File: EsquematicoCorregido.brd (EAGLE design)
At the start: 100 x 80 mm, 42 parts, among them IC1 OPA991TIDCKR, IC10 MCP73831T-2ACI_OT, IC2 AD8226ARZ-RL, IC3 OPA991TIDCKR, IC4 ESP32-S3-WROOM-1-N16R8, IC5 OPA991TIDCKR, IC6 MAX30102EFD+T, IC7 LP38692MP-3.3_NOPB, IC8 LP38692MP-1.8_NOPB, IC9 REF2033AIDDCT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

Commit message: ultimas actualizaciones
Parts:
- removed C7: C0805J104K1RACAUTO, C0805J104K1RACAUTO:CAPC2012X140N
- removed U1: DM-OLED096-636, DM-OLED096-636:MODULE_DM-OLED096-636
- added SV1: (no value), con-lstb:MA04-1
- C2, C5, C6: value QXK2E475KTP -> (none); device QXK2E475KTP:QXK2E475KTP -> rcl:C0805
- C4: value C2220X205K1RLCAUTO -> (none); device C2220X205K1RLCAUTO:CAPC5950X340N -> rcl:C0805
- C8: value C0805J104K1RACAUTO -> (none); device C0805J104K1RACAUTO:CAPC2012X140N -> rcl:C0805
- moved C8 243.1 mm to (-149.9, -113.0)
- moved S4 238.7 mm to (40.6, 64.8)
- moved S3 234.8 mm to (40.6, 73.7)
- moved C4 216.6 mm to (-149.9, -102.9)
- moved C6 207.9 mm to (-149.9, -108.0)
- moved C5 189.7 mm to (-149.9, -118.1)
- moved POWER 173.4 mm to (48.3, 8.89)
- moved BATT 168.5 mm to (30.5, 10.2)
- moved C2 158.6 mm to (-149.9, -97.8)
- moved IC5 114.4 mm to (33.0, 40.6)
- moved J1 104.2 mm to (2.16, 55.4), turned to 270 degrees
- moved IC10 96.0 mm to (19.1, 7.62)
- moved IC3 95.2 mm to (25.4, 40.6)
- moved IC8 52.1 mm to (21.6, 19.1)
- moved IC7 49.7 mm to (36.8, 19.1)
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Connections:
- new net N$21: SV1.1
- net +3V3: now also C4.1, C6.1, SV1.2; no longer C6.2, C8.2, U1.2
- net EN: now also S3.3
- net GND: now also C5.2, C8.2, S3.1, S4.1; no longer C5.1, C7.1, U1.1
- net IO0: now also S4.3
- net N$2: now also C12.2; no longer C2.2
- net N$3: now also C12.1; no longer C2.1
- net N$4: now also C2.2; no longer C4.2
- net N$9: now also C4.2, C6.2; no longer C6.1, C8.1
- net SCL_DSP: now also SV1.4; no longer U1.3
- net SDA_DSP: now also SV1.3; no longer U1.4
- net VDD: now also C5.1, C8.1; no longer C5.2, C7.2
- net VSS: now also C2.1; no longer C4.1
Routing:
- net +3V3: track 18.5 -> 2.50 mm
- net N$3: track 3.81 -> 0.00 mm
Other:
- board size 100 x 80 mm -> 70.9 x 80 mm

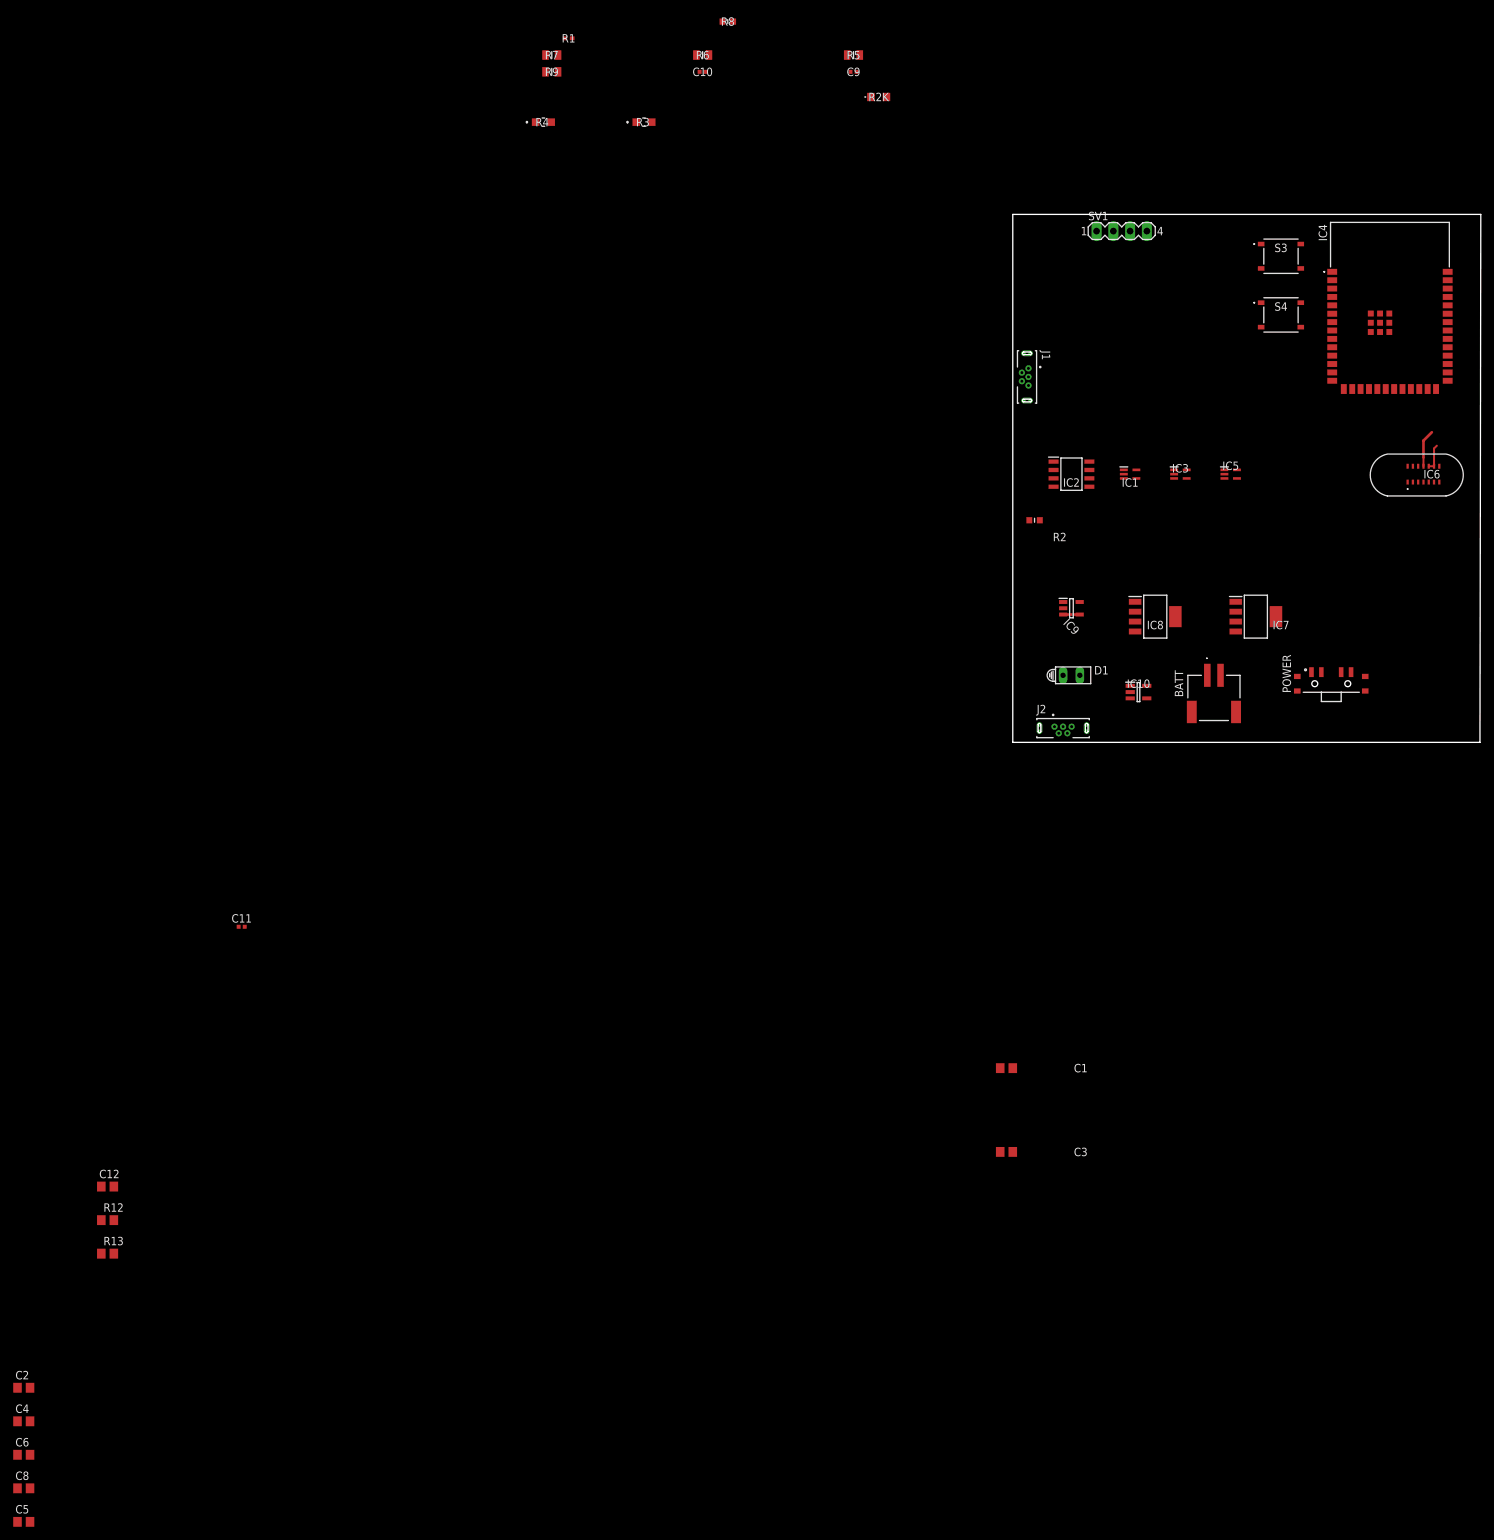
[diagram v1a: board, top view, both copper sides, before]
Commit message: fix: PCB and schematic errors fixed
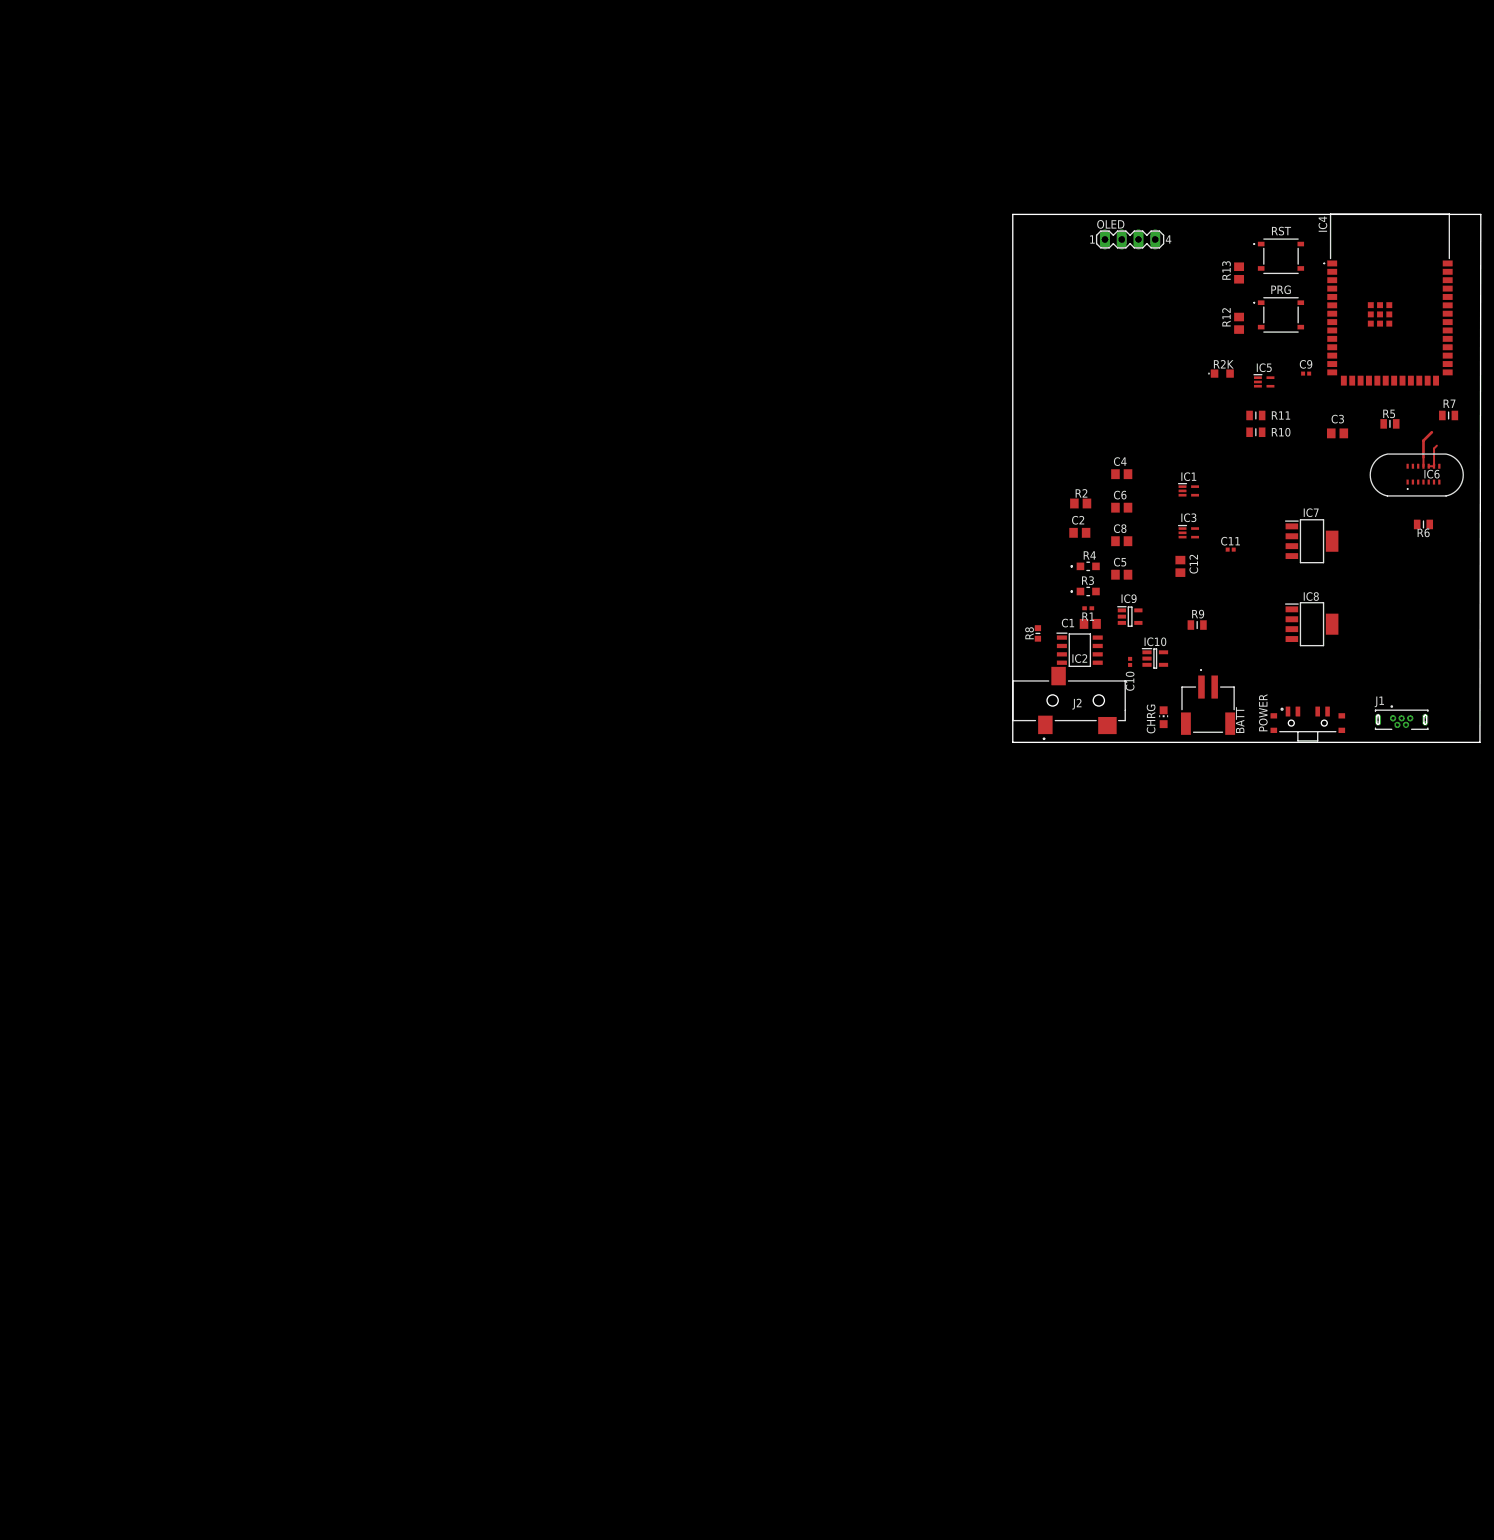
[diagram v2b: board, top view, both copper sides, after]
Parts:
- removed D1: HLMP6, display-hp:HLMP6
- removed SV1: (no value), con-lstb:MA04-1
- added CHRG: (no value), led:CHIP-LED0805
- added OLED: (no value), con-lstb:MA04-1
- added R10, R11: CRCW0805220RFKTAHP, CRCW0805220RFKTAHP:RESC2012X60N
- J2: value USB3131-30-0230-A_REVB -> SJ-3523-SMT-TR; device USB3131-30-0230-A_REVB:GCT_USB3131-30-0230-A_REVB -> SJ-3523-SMT-TR:SJ3523SMTTR
- R2: value RN73H1JTTD1043B50 -> (none); device RN73H1JTTD1043B50:RESC1608X55N -> rcl:R0805
- moved R13 226.9 mm to (34.3, 71.1), turned to 270 degrees
- moved C4 219.7 mm to (16.5, 40.6)
- moved C5 219.7 mm to (16.5, 25.4)
- moved C6 219.7 mm to (16.5, 35.6)
- moved C8 219.7 mm to (16.5, 30.5)
- moved R12 218.8 mm to (34.3, 63.5), turned to 90 degrees
- moved C2 205.9 mm to (10.2, 31.8)
- moved C12 187.8 mm to (25.4, 26.7), turned to 270 degrees
- moved C11 160.4 mm to (33.0, 29.2)
- moved R7 146.5 mm to (66.0, 49.5)
- moved R6 130.3 mm to (62.2, 33.0), turned to 180 degrees
- moved R9 128.8 mm to (27.9, 17.8)
- moved C3 119.9 mm to (49.2, 46.8), turned to 180 degrees
- moved R1 116.9 mm to (11.4, 20.3), turned to 180 degrees
- moved C10 110.4 mm to (17.8, 12.2), turned to 270 degrees
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- renumbered S3 to RST, S4 to PRG
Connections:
- removed net 5V: J2.1
- removed net N$15: IC2.4
- removed net N$16: D1.K, R9.2
- new net INA+: IC2.4, J2.3
- new net INA-: IC2.1, J2.2
- new net N$5: IC5.4, R10.1, R11.1
- net +3V3: now also OLED.2; no longer J1.1, SV1.2
- net +5V: now also CHRG.A, J1.1; no longer D1.A
- net GND: now also R11.2; no longer J2.5, J2.S1, J2.S2
- net N$14: now also CHRG.C, R9.2; no longer IC2.1
- net N$21: now also OLED.1; no longer SV1.1
- net OUT-ADC: now also R10.2
- net SCL_DSP: now also OLED.4; no longer SV1.4
- net SDA_DSP: now also OLED.3; no longer SV1.3
- net VSS: now also J2.1
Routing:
- net +3V3: track 2.50 -> 0.00 mm

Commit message: Avance PCB
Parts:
- removed J1: USB3131-30-0230-A_REVB, USB3131-30-0230-A_REVB:GCT_USB3131-30-0230-A_REVB
- removed R2K: ERJ-UP6D2001V, ERJ-UP6D2001V:ERJUP6
- added J3: USB4216-03-A, USB4216-03-A:USB421603A
- added R14, R15, R16: (no value), rcl:R0805
- C10, C11, C9: value GRM155C80G106ME18D -> (none); device GRM155C80G106ME18D:CAPC1005X70N -> rcl:C0805
- R1: value RN73H1ETTP4812D25 -> (none); device RN73H1ETTP4812D25:RESC1005X40N -> rcl:R0805
- R9: value CRCW0805220RFKTAHP -> (none); device CRCW0805220RFKTAHP:RESC2012X60N -> rcl:R0805
- moved R5 3.97 mm to (61.1, 48.8), turned to 270 degrees
- moved IC7 3.81 mm to (45.3, 26.7)
- moved IC8 2.54 mm to (45.3, 15.4)
- moved C10 1.02 mm to (16.8, 12.1), turned to 90 degrees
- moved R7 0.97 mm to (65.7, 48.6), turned to 270 degrees
- moved C11 0.80 mm to (32.8, 28.4)
- moved C9 0.51 mm to (44.5, 55.4)
- moved R1 0.38 mm to (11.8, 20.3), turned to 0 degrees
- moved R12 0.38 mm to (34.3, 63.9)
- moved R13 0.36 mm to (34.0, 70.9)
- turned IC6 to 270 degrees
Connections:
- removed net N$10: IC4.3
- new net N$16: J3.A5, R15.1
- new net N$19: J3.B5, R16.2
- net +3V3: now also R12.2, R13.2
- net +5V: now also C9.1, J3.A4, J3.B4; no longer C9.2, J1.1
- net 3V3: now also C11.2; no longer C11.1, R12.2, R13.2
- net BATT+: now also C10.1; no longer C10.2
- net D+: now also J3.A6, J3.B6; no longer J1.3
- net D-: now also J3.A7, J3.B7; no longer J1.2
- net EN: now also IC4.3
- net GND: now also C10.2, C11.1, C9.2, J3.A1, J3.B1, J3.G1, J3.G2, J3.G3, J3.G4, R14.1, R15.2, R16.1; no longer C10.1, C11.2, C9.1, J1.5, J1.S1, J1.S2, R2K.1
- net N$17: now also R14.2; no longer R2K.2
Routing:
- net EN: track 0.00 -> 16.1 mm
- net VDD: track 5.68 -> 0.00 mm
- net IO0: track 0.00 -> 5.25 mm
- net N$9: track 4.10 -> 0.00 mm
- net N$15: track 0.00 -> 1.78 mm
- added copper zone on layer 1, net GND
- added copper zone on layer 16, net GND

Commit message: modificaciones PCB
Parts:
- moved C9 44.3 mm to (30.1, 13.5)
- moved R14 43.5 mm to (36.8, 12.7), turned to 270 degrees
- moved C11 37.6 mm to (23.0, 64.8), turned to 90 degrees
- moved C3 32.4 mm to (19.0, 35.1)
- moved C5 29.6 mm to (45.5, 31.4), turned to 180 degrees
- moved C8 29.1 mm to (45.5, 27.7), turned to 180 degrees
- moved C4 29.0 mm to (45.5, 38.9)
- moved C6 29.0 mm to (45.5, 35.3)
- moved OLED 25.4 mm to (19.1, 50.8)
- moved IC1 20.4 mm to (6.35, 39.4)
- moved C12 17.4 mm to (8.64, 31.4), turned to 0 degrees
- moved IC5 17.0 mm to (30.5, 39.4)
- moved R3 15.3 mm to (12.7, 38.1)
- moved R1 14.7 mm to (10.5, 34.9)
- moved R11 14.2 mm to (34.3, 35.6)
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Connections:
- net VDD renamed +1V8
- removed net N$21: OLED.1
- net GND: now also OLED.1
- net OUTFILT: no longer IC4.20
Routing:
- net +3V3: track 0.00 -> 111.3 mm, vias 0 -> 2
- net SDA_DSP: track 0.00 -> 47.3 mm
- net +1V8: track 0.00 -> 45.1 mm, vias 0 -> 2
- net SDA: track 0.00 -> 40.7 mm
- net SCL_DSP: track 0.00 -> 37.4 mm, vias 0 -> 2
- net IO0: track 5.25 -> 42.3 mm, vias 0 -> 2
- net N$12: track 0.00 -> 31.0 mm
- net SCL: track 0.00 -> 30.5 mm, vias 0 -> 2
- net VSS: track 0.00 -> 26.6 mm
- net N$9: track 0.00 -> 24.9 mm, vias 0 -> 2
- net N$8: track 0.00 -> 18.3 mm
- net OUTFILT: track 0.00 -> 17.2 mm, vias 0 -> 2
- net N$4: track 0.00 -> 16.1 mm, vias 0 -> 2
- net COMM: track 0.00 -> 15.4 mm
- net PPG: track 0.00 -> 13.2 mm
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
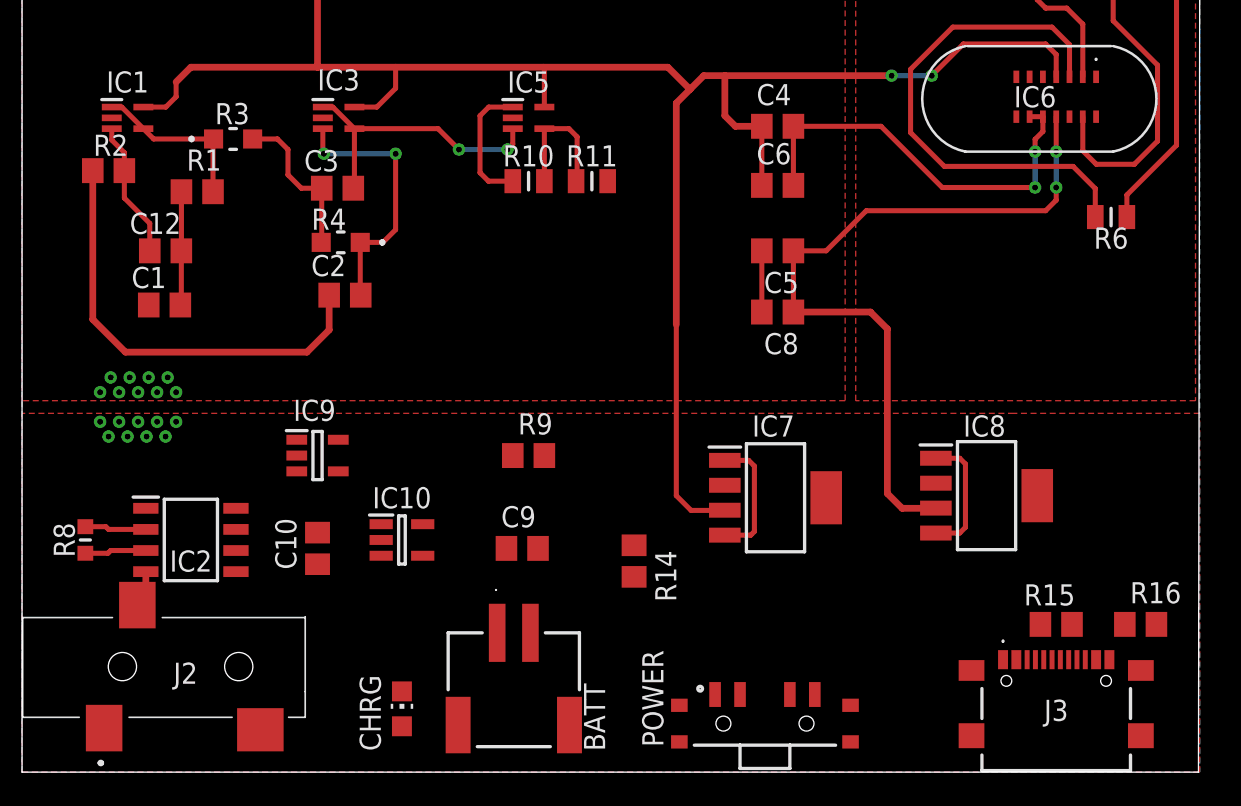
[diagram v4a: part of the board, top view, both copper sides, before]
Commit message: Mas pistas a la PCB
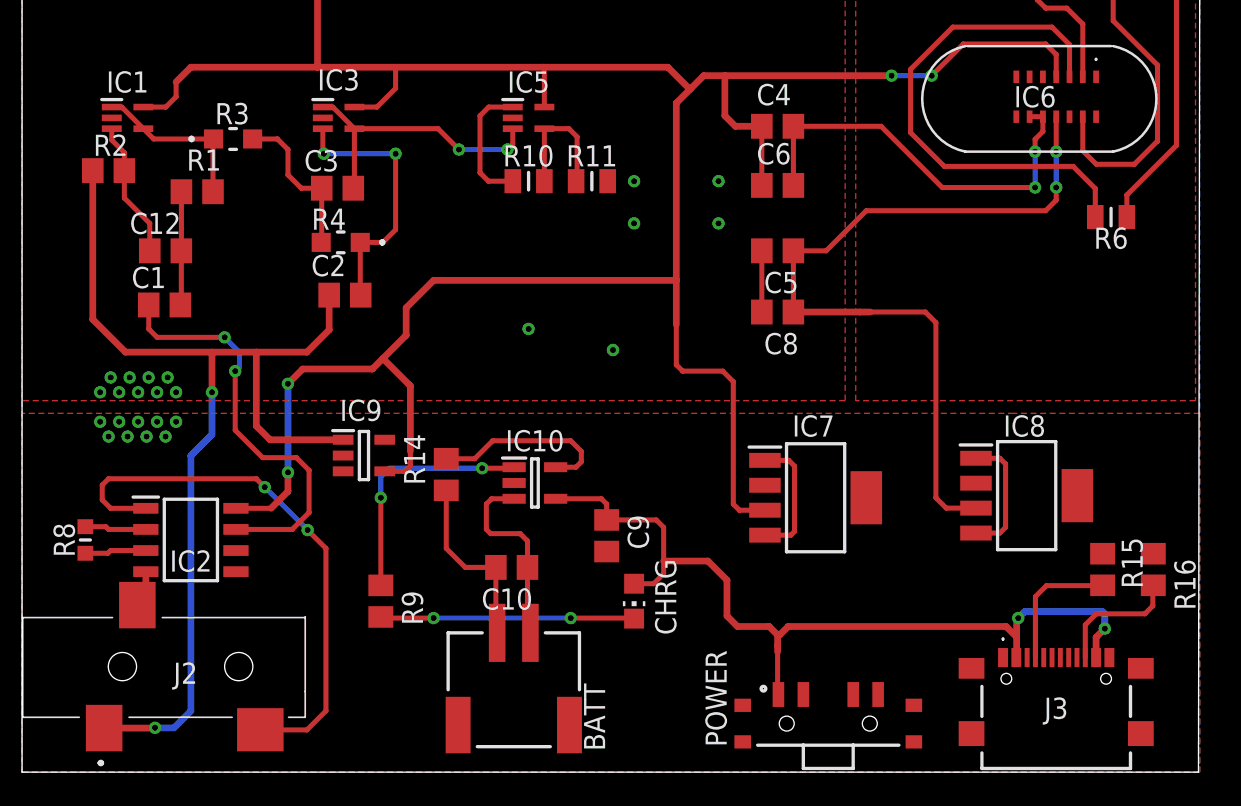
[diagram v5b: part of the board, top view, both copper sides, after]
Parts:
- moved CHRG 15.4 mm to (36.8, 10.3), turned to 180 degrees
- moved R9 12.5 mm to (21.6, 10.3), turned to 270 degrees
- moved R14 12.4 mm to (25.5, 17.9), turned to 90 degrees
- moved C10 11.7 mm to (29.5, 12.3), turned to 180 degrees
- moved IC10 8.70 mm to (30.9, 17.4)
- moved C9 5.14 mm to (35.2, 14.2), turned to 270 degrees
- moved R15 4.33 mm to (65.0, 12.2), turned to 90 degrees
- moved POWER 3.81 mm to (48.5, 2.92)
- moved R16 3.39 mm to (68.1, 12.2), turned to 270 degrees
- moved IC9 2.79 mm to (20.6, 19.1)
- moved IC7 2.41 mm to (47.8, 16.5)
- moved IC8 2.41 mm to (60.5, 16.6)
- moved J3 0.13 mm to (62.2, 3.56)
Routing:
- net +5V: track 0.00 -> 51.7 mm, vias 0 -> 2
- net +3V3: track 111.3 -> 159.2 mm, vias 2 -> 4
- net VSS: track 26.6 -> 64.4 mm, vias 0 -> 2
- net INA-: track 0.00 -> 33.3 mm, vias 0 -> 2
- net INA: track 0.00 -> 25.1 mm, vias 0 -> 2
- net N$14: track 0.00 -> 15.8 mm, vias 0 -> 2
- net N$18: track 0.00 -> 14.8 mm, vias 0 -> 2
- net BATT+: track 0.00 -> 11.7 mm
- net N$17: track 0.00 -> 11.2 mm
- net GND: track 3.68 -> 14.6 mm, vias 18 -> 24
- net N$16: track 0.00 -> 8.42 mm
- net N$19: track 0.00 -> 7.75 mm
- net +1V8: track 45.1 -> 48.5 mm
